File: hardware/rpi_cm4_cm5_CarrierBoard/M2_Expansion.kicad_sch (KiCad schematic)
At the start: 17 parts, among them J23 MDT420M03001, U38 ASAK-32.768KHZ-LRS-T

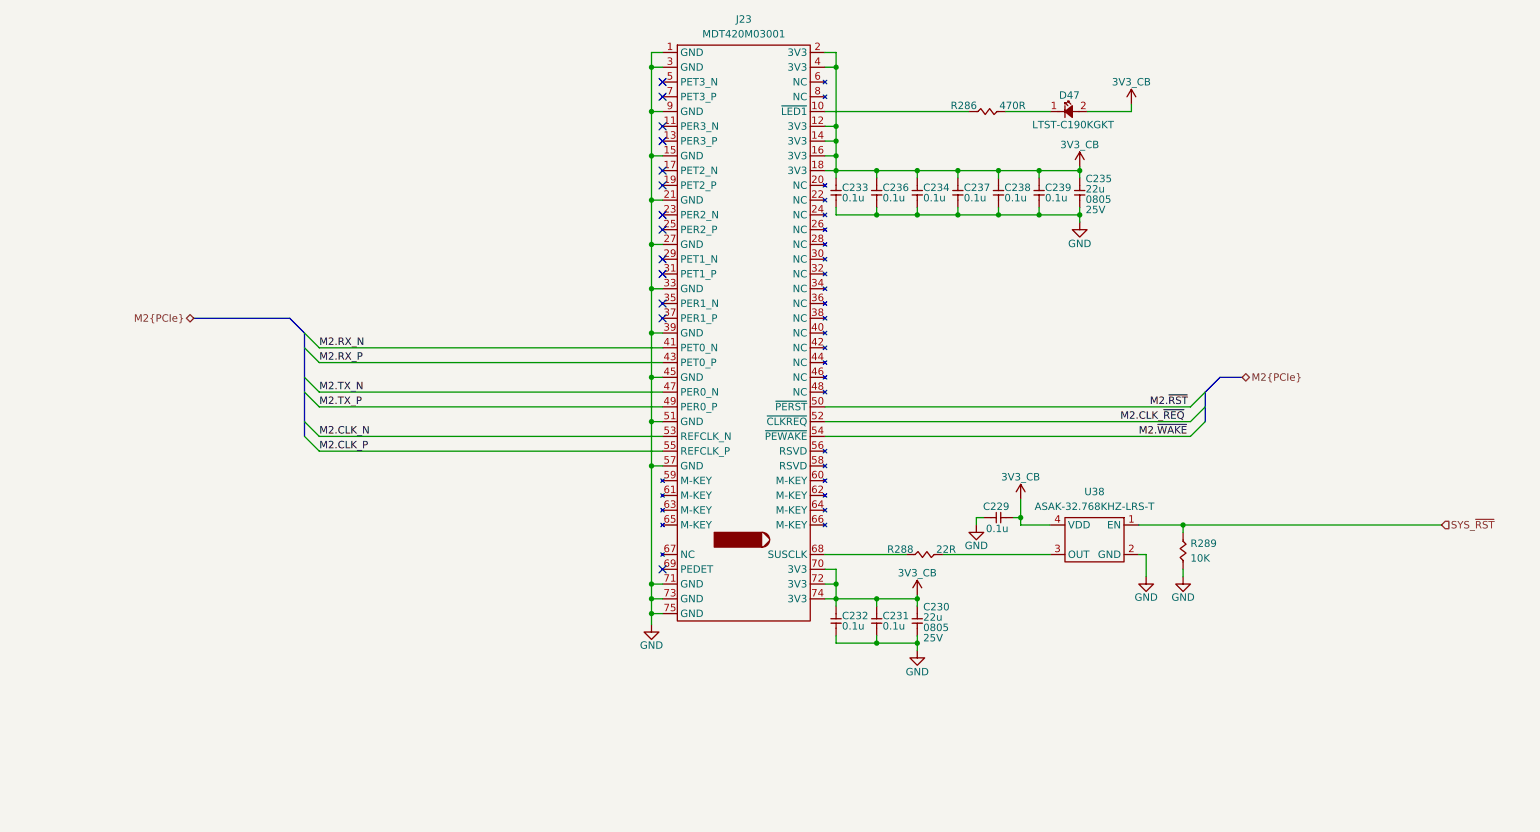
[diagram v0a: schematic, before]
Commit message: Add preliminary BOM and preliminary .pdf schmematics Add BOM option for I2C control of ILI2132A for CapTouch HMI Add BOM options and DNP / 0R resistors for CM4 - CM5 build options
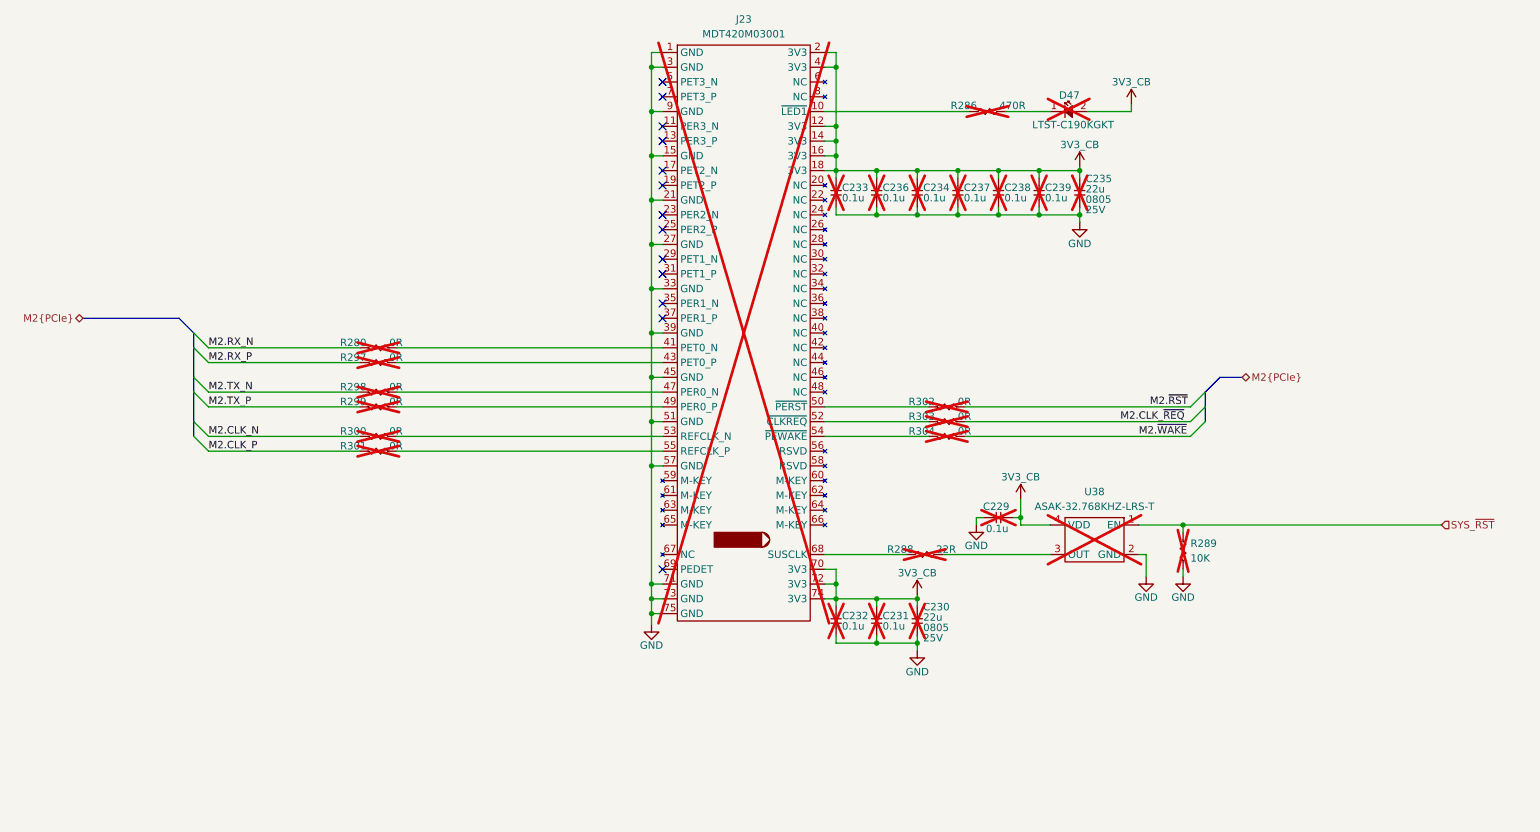
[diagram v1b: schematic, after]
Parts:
- added R280, R297, R298, R299, R300, R301, R302, R303, R304: 0R, footprint:RES_0402, symbol KicadCompDb:Resistors/RES_SMT_00001
- C229, C230, C231, C232, C233, C234, C235, C236, C237, C238, C239, D47, J23, R286, R288, R289, U38: now not fitted
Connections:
- net M2.CLK_N: now also R300.2; no longer J23.53 (REFCLK_N)
- net M2.CLK_P: now also R301.2; no longer J23.55 (REFCLK_P)
- net M2.CLK_~{REQ}: now also R303.1; no longer J23.52 (~{CLKREQ})
- net M2.RX_N: now also R280.2; no longer J23.41 (PET0_N)
- net M2.RX_P: now also R297.2; no longer J23.43 (PET0_P)
- net M2.TX_N: now also R298.2; no longer J23.47 (PER0_N)
- net M2.TX_P: now also R299.2; no longer J23.49 (PER0_P)
- net M2.~{RST}: now also R302.1; no longer J23.50 (~{PERST})
- net M2.~{WAKE}: now also R304.1; no longer J23.54 (~{PEWAKE})
- new net: J23.50 (~{PERST}), R302.2
- new net: J23.54 (~{PEWAKE}), R304.2
- new net: J23.55 (REFCLK_P), R301.1
- new net: J23.41 (PET0_N), R280.1
- new net: J23.43 (PET0_P), R297.1
- new net: J23.47 (PER0_N), R298.1
- new net: J23.49 (PER0_P), R299.1
- new net: J23.52 (~{CLKREQ}), R303.2
- new net: J23.53 (REFCLK_N), R300.1

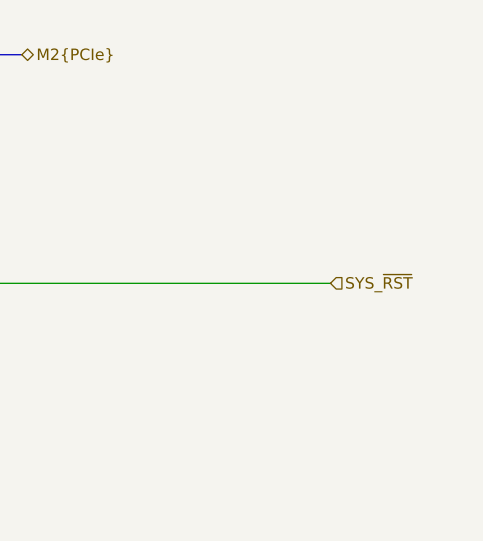
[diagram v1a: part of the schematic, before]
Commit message: Added power input protection & filter Added dedicated QWIIC connector on RPI CMx I2C6 bus Adjusted power table and PinMux Updated schematics accordingly
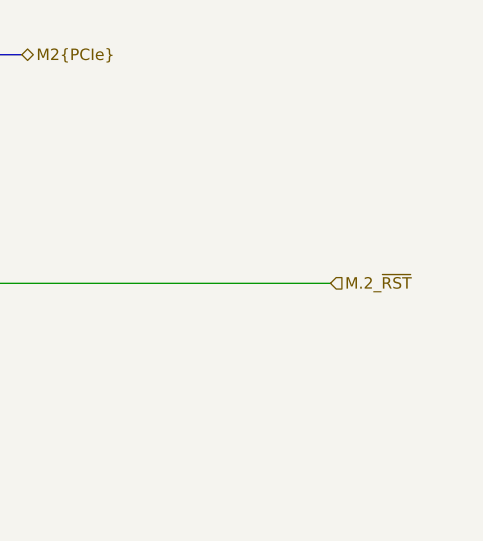
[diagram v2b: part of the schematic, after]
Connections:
- net SYS_~{RST} renamed M.2_~{RST}
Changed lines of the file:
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@@
 		)
 	)
-	(hierarchical_label "SYS_~{RST}"
+	(hierarchical_label "M.2_~{RST}"
 		(shape input)
 		(at 263.525 130.175 0)

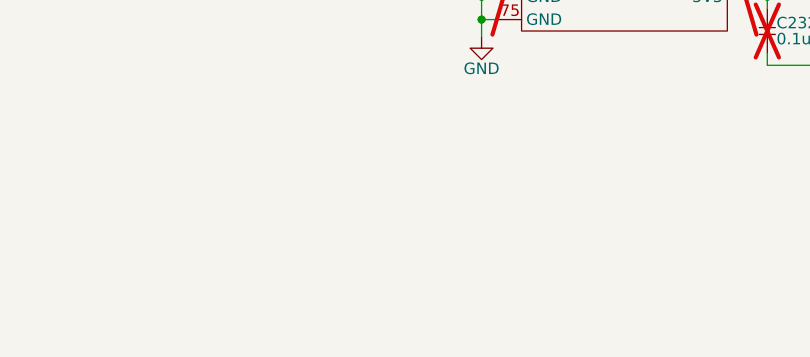
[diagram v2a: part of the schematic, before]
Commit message: Update watchdog timer circuit to add external watchdog timer IC to be fed by PIC Adjust reset scheme in power supply sheet accordingly Adjust PinMux, regen BOM and PDF schematics (preliminary) Start preliminary component placement in the PCB
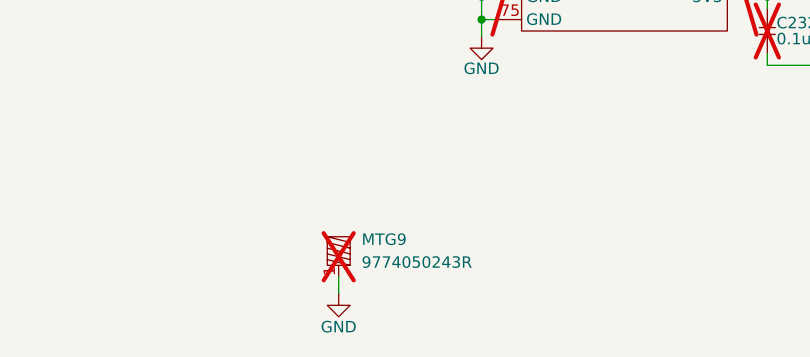
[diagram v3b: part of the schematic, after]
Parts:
- added MTG9: 9774050243R, footprint:9774050243R, symbol KicadCompDb:Miscellaneous/MISC_00008
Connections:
- net GND: now also MTG9.1
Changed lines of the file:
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@@
 	(wire
 		(pts
+			(xy 111.76 173.99) (xy 111.76 175.895)
+		)
+		(stroke
+			(width 0)
+			(type default)
+		)
+	)
+	(wire
+		(pts
 			(xy 157.48 64.135) (xy 159.385 64.135)
 		)
@@
 	)
 	(symbol
+		(lib_id "KiCad_Pwr_Symbols:GND")
+		(at 111.76 175.895 0)
+		(mirror y)
+		(unit 1)
+		(exclude_from_sim no)
+		(in_bom yes)
+		(on_board yes)
+		(dnp no)
+		(property "Reference" "#PWR0414"
+			(at 111.76 182.245 0)
+			(effects
+				(font
+					(size 1.27 1.27)
+				)
+				(hide yes)
+			)
+		)
+		(property "Value" "GND"
+			(at 111.76 179.578 0)
+			(effects
+				(font
+					(size 1.27 1.27)
+				)
+			)
+		)
+		(property "Footprint" ""
+			(at 111.76 175.895 0)
+			(effects
+				(font
+					(size 1.27 1.27)
+				)
+				(hide yes)
+			)
+		)
+		(property "Datasheet" ""
+			(at 111.76 175.895 0)
+			(effects
+				(font
+					(size 1.27 1.27)
+				)
+				(hide yes)
+			)
+		)
+		(property "Description" "Power symbol creates a global label with name \"GND\" , ground"
+			(at 111.76 175.895 0)
+			(effects
+				(font
+					(size 1.27 1.27)
+				)
+				(hide yes)
+			)
+		)
+		(pin "1"
+		)
+		(instances
+			(project "rpi_cm4_cm5_CarrierBoard"
+				(path "/7dcdf741-90ca-4333-848c-806f4d64158e/9de20a6e-0c13-4cd2-9bfa-6170acf466d0"
+					(reference "#PWR0414")
+					(unit 1)
+				)
+			)
+		)
+	)
+	(symbol
 		(lib_id "KicadCompDb:Capacitors/CAP_CER_SMT_00001")
 		(at 180.34 75.565 90)
@@
 					(unit 1)
 				)
+			)
+		)
+	)
+	(symbol
+		(lib_id "KicadCompDb:Miscellaneous/MISC_00008")
+		(at 110.49 169.545 0)
+		(unit 1)
+		(exclude_from_sim no)
+		(in_bom yes)
+		(on_board yes)
+		(dnp yes)
+		(fields_autoplaced yes)
+		(property "Reference" "MTG9"
+			(at 114.3 169.8624 0)
+			(effects
+				(font
+					(size 1.27 1.27)
+				)
+				(justify left)
+			)
+		)
+		(property "Value" "9774050243R"
+			(at 114.3 172.4024 0)
+			(effects
+				(font
+					(size 1.27 1.27)
+				)
+				(justify left)
+			)
+		)
+		(property "Footprint" "footprint:9774050243R"
+			(at 110.49 169.545 0)
+			(effects
+				(font
+					(size 1.27 1.27)
+				)
+				(hide yes)
+			)
+		)
+		(property "Datasheet" ""
+			(at 110.49 169.545 0)
+			(effects
+				(font
+					(size 1.27 1.27)
+				)
+				(hide yes)
+			)
+		)
+		(property "Description" "ROUND STANDOFF M2X0.4 STEEL 5MM"
+			(at 110.49 169.545 0)
+			(effects
+				(font
+					(size 1.27 1.27)
+				)
+				(hide yes)
+			)
+		)
+		(property "Type" "ROUND STANDOFF M2X0.4 STEEL 5MM"
+			(at 110.49 169.545 0)
+			(show_name yes)
+			(effects
+				(font
+					(size 1.27 1.27)
+				)
+				(hide yes)
+			)
+		)
+		(property "Package" "M2x0.4"
+			(at 110.49 169.545 0)
+			(show_name yes)
+			(effects
+				(font
+					(size 1.27 1.27)
+				)
+				(hide yes)
+			)
+		)
+		(property "Operating Temperature" "-40°C ~ 150°C"
+			(at 110.49 169.545 0)
+			(show_name yes)
+			(effects
+				(font
+					(size 1.27 1.27)
+				)
+				(hide yes)
+			)
+		)
+		(property "Dimensions" "4.35mm x 6.40mm"
+			(at 110.49 169.545 0)
+			(show_name yes)
+			(effects
+				(font
+					(size 1.27 1.27)
+				)
+				(hide yes)
+			)
+		)
+		(property "Manufacturer" "Würth Elektronik"
+			(at 110.49 169.545 0)
+			(show_name yes)
+			(effects
+				(font
+					(size 1.27 1.27)
+				)
+				(hide yes)
+			)
+		)
+		(property "Manufacturer Part Number" "9774050243R"
+			(at 110.49 169.545 0)
+			(show_name yes)
+			(effects
+				(font
+					(size 1.27 1.27)
+				)
+				(hide yes)
+			)
+		)
+		(property "Distributor" "DigiKey"
+			(at 110.49 169.545 0)
+			(show_name yes)
+			(effects
+				(font
+					(size 1.27 1.27)
+				)
+				(hide yes)
+			)
+		)
+		(property "Distributor Part Number" "732-7097-1-ND"
+			(at 110.49 169.545 0)
+			(show_name yes)
+			(effects
+				(font
+					(size 1.27 1.27)
+				)
+				(hide yes)
+			)
+		)
+		(pin "1"
+		)
+		(instances
+			(project ""
+				(path "/7dcdf741-90ca-4333-848c-806f4d64158e/9de20a6e-0c13-4cd2-9bfa-6170acf466d0"
+					(reference "MTG9")
+					(unit 1)
+				)

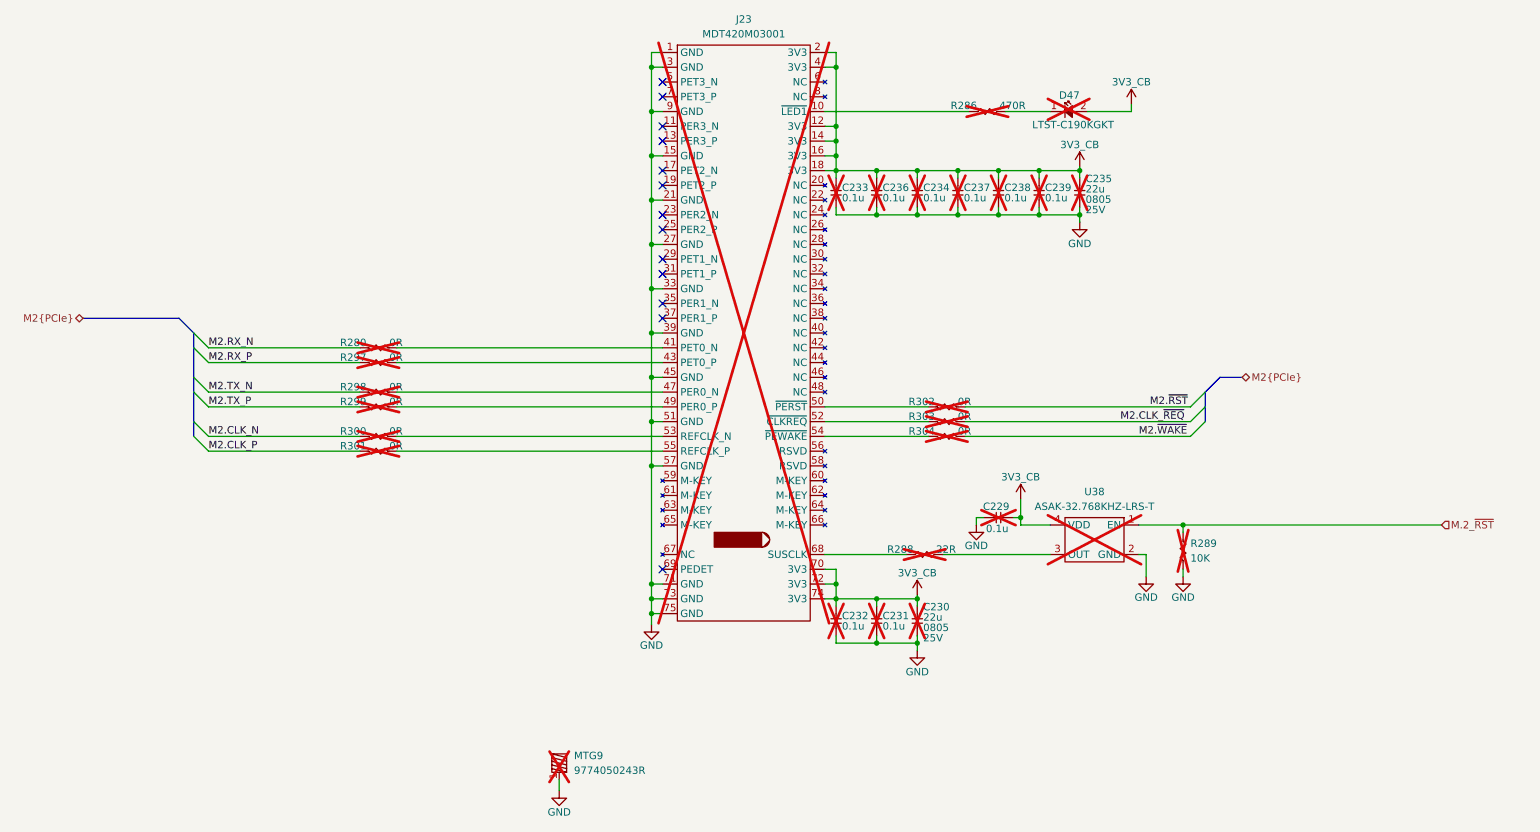
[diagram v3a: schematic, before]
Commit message: Update schematics based on PCB preliminary placement Add preliminary design rules to PCB
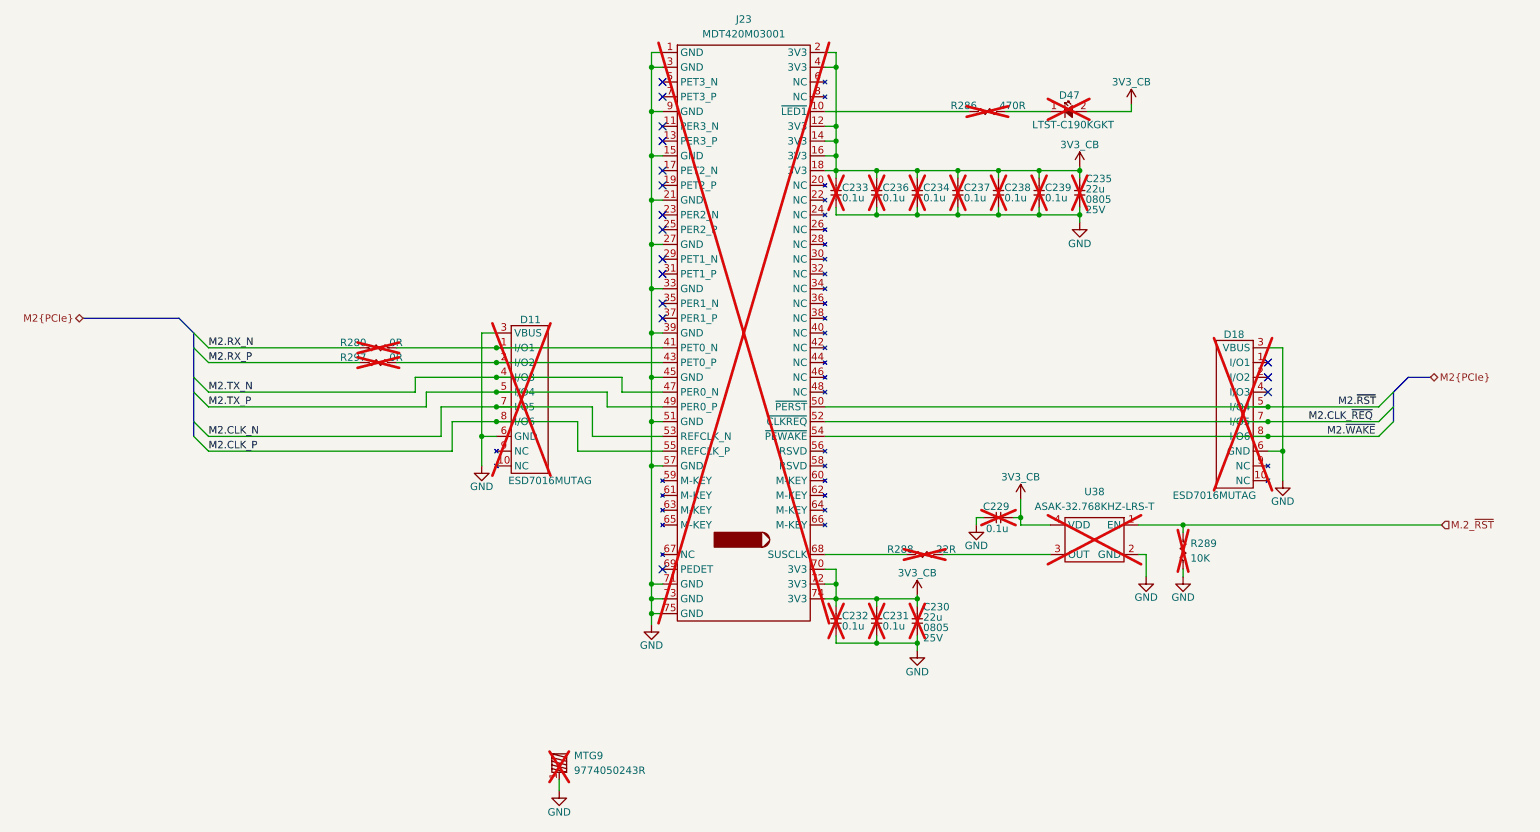
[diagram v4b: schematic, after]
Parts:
- removed R298, R299, R300, R301, R302, R303, R304: 0R, footprint:RES_0402, symbol KicadCompDb:Resistors/RES_SMT_00001
- added D11, D18: ESD7016MUTAG, footprint:UDFN8, symbol KicadCompDb:ESD Diodes/ESD_DIODE_00001
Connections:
- net GND: now also D11.3 (VBUS), D11.6 (GND), D18.3 (VBUS), D18.6 (GND)
- net M2.CLK_N: now also J23.53 (REFCLK_N), D11.7 (I/O5)
- net M2.CLK_P: now also J23.55 (REFCLK_P), D11.8 (I/O6)
- net M2.CLK_~{REQ}: now also J23.52 (~{CLKREQ}), D18.7 (I/O5)
- net M2.TX_N: now also J23.47 (PER0_N), D11.4 (I/O3)
- net M2.TX_P: now also J23.49 (PER0_P), D11.5 (I/O4)
- net M2.~{RST}: now also J23.50 (~{PERST}), D18.5 (I/O4)
- net M2.~{WAKE}: now also J23.54 (~{PEWAKE}), D18.8 (I/O6)
- net at J23.41 (PET0_N), R280.1: now also D11.1 (I/O1)
- net at J23.43 (PET0_P), R297.1: now also D11.2 (I/O2)
- no-connect marks 13 -> 16

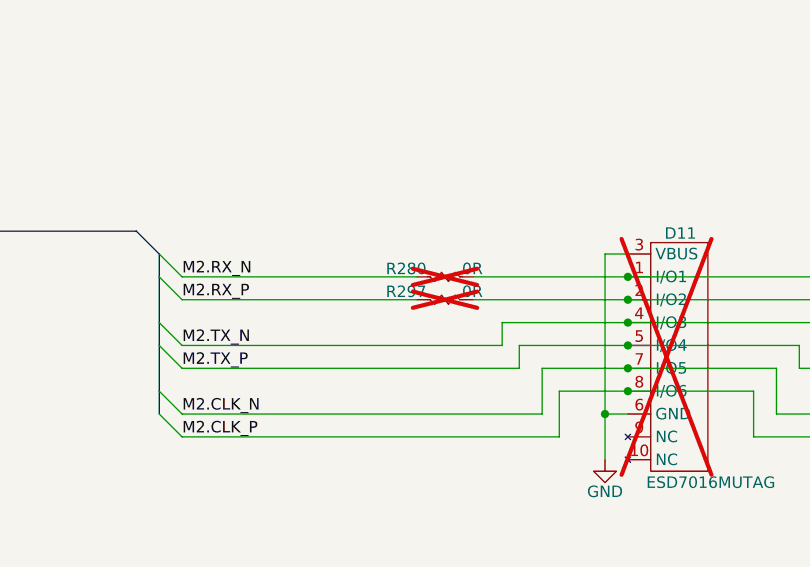
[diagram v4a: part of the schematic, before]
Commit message: Update PCB design rules for outer layers differential pairs Update preliminary component placement Update schematics based on PCB placement & remove duplicata / unnecessary components Update design notes and power table
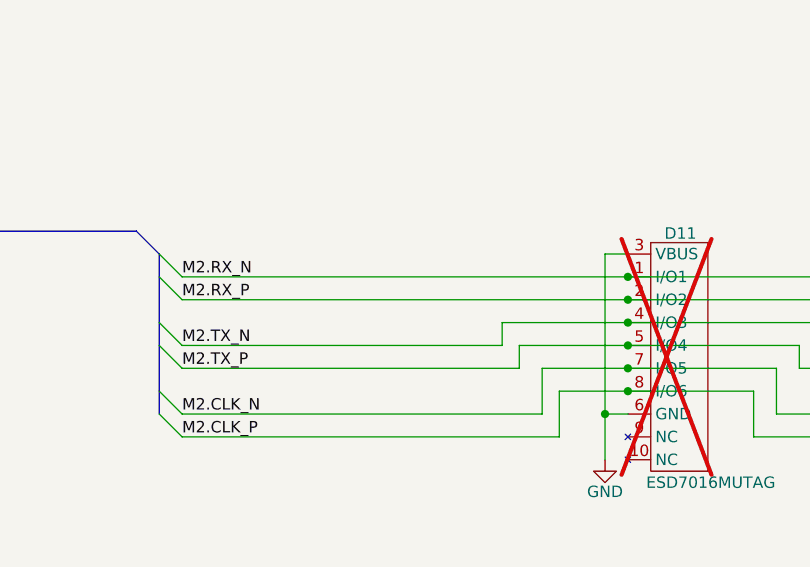
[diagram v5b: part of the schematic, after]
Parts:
- removed R280, R297: 0R, footprint:RES_0402, symbol KicadCompDb:Resistors/RES_SMT_00001
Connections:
- net M2.RX_N: now also D11.1 (I/O1), J23.41 (PET0_N)
- net M2.RX_P: now also D11.2 (I/O2), J23.43 (PET0_P)
